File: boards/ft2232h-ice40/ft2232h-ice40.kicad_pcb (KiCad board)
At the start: 4 copper layers, 34 x 22.4 mm, 36 parts, among them J1 USB_B_Micro, J2 Conn_01x08, U1 AP7361C_SOT-89-5, U2 FT2232H, X1 ASEM1-12.000MHZ

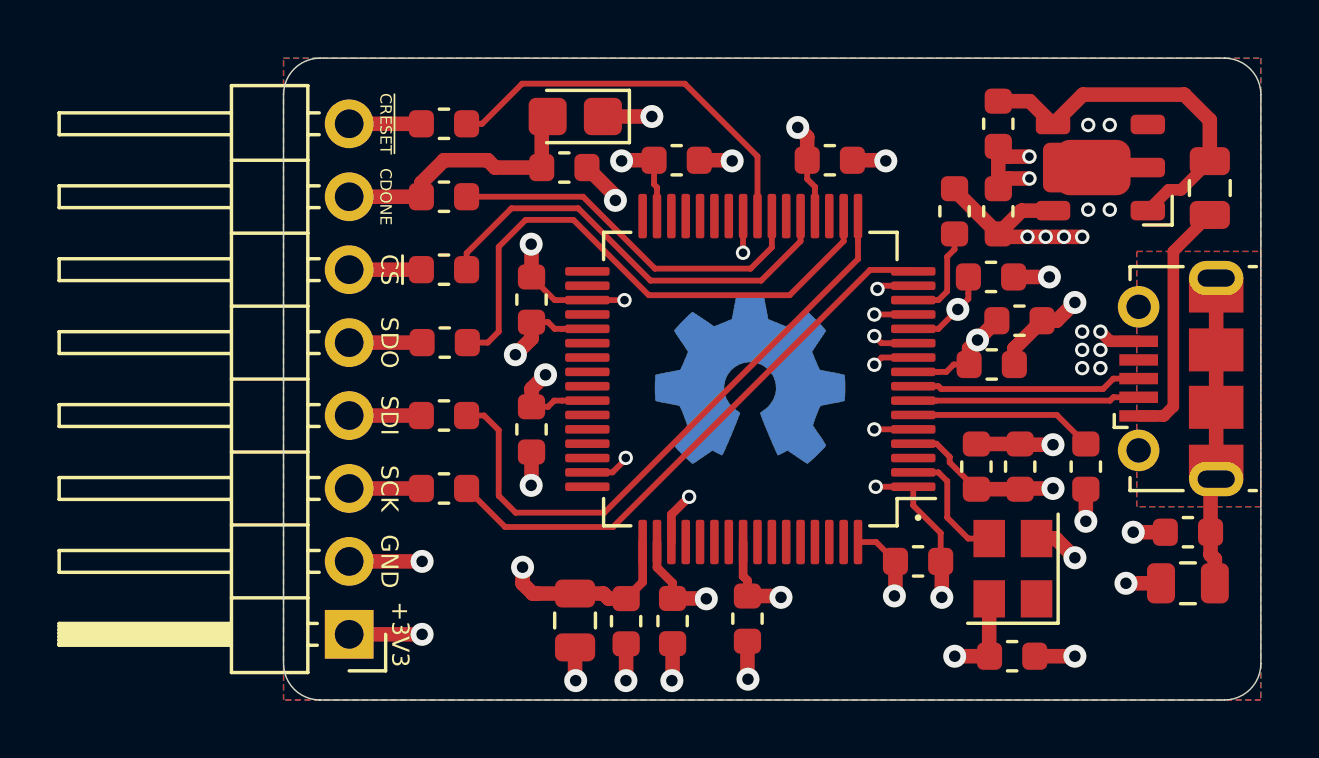
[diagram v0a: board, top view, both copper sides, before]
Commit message: Minor tweaks to signal layout.
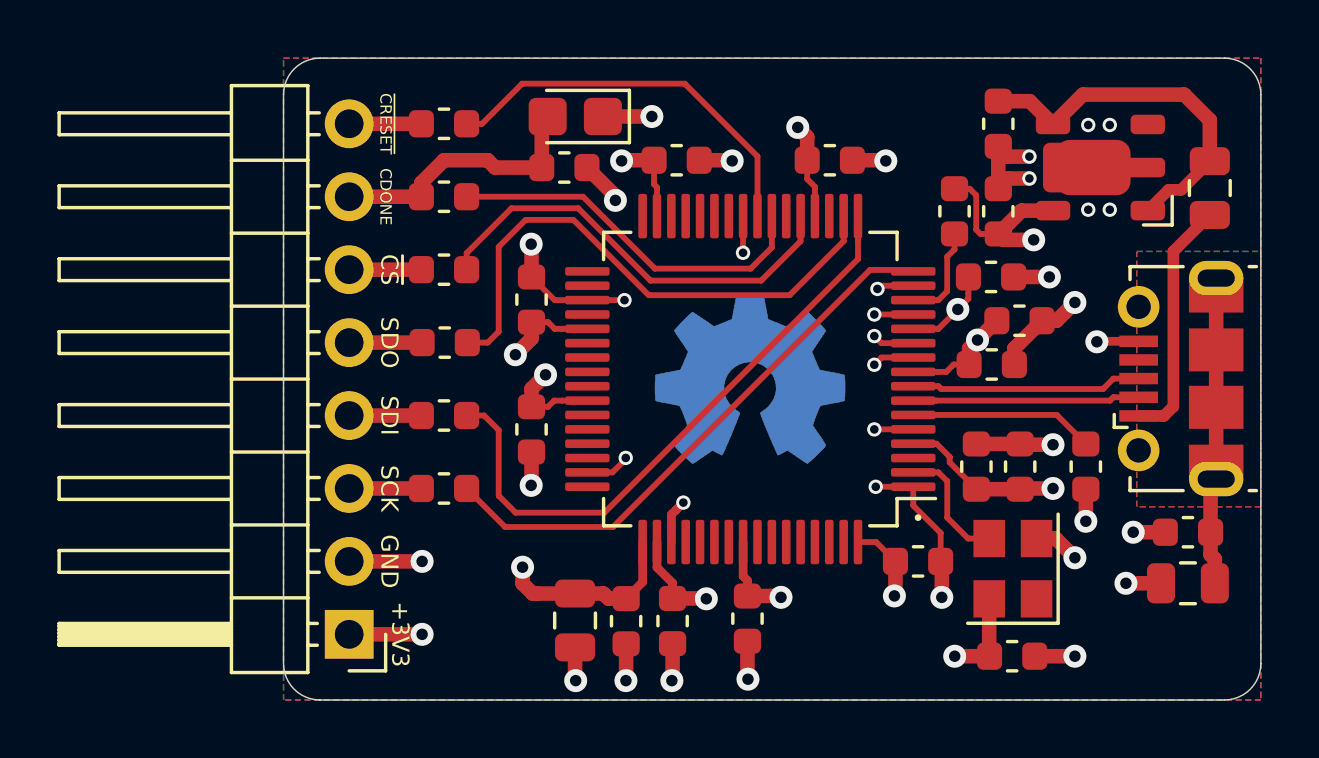
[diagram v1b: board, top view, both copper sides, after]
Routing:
- net +3V3: track 40.7 -> 39.7 mm, vias 14 -> 11
- net GND: track 55.5 -> 55.2 mm, vias 41 -> 36
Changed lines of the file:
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@@
     (thickness 1.6)
     (drawings 17)
-    (tracks 310)
+    (tracks 305)
     (zones 0)
     (modules 36)
@@
   )
   (setup
-    (last_trace_width 0.508)
+    (last_trace_width 0.2032)
     (user_trace_width 0.2032)
     (user_trace_width 0.3048)
@@
   (segment (start 76.2 26.416) (end 76.835 25.781) (width 0.508) (layer F.Cu) (net 1))
   (segment (start 75.692 26.416) (end 76.2 26.416) (width 0.508) (layer F.Cu) (net 1))
-  (via (at 77.724 28.067) (size 0.5) (drill 0.3) (layers F.Cu B.Cu) (net 1))
-  (via (at 77.724 27.432) (size 0.5) (drill 0.3) (layers F.Cu B.Cu) (net 1))
-  (via (at 77.089 26.797) (size 0.5) (drill 0.3) (layers F.Cu B.Cu) (net 1))
-  (via (at 77.089 27.432) (size 0.5) (drill 0.3) (layers F.Cu B.Cu) (net 1))
-  (via (at 77.089 28.067) (size 0.5) (drill 0.3) (layers F.Cu B.Cu) (net 1))
-  (via (at 77.724 26.797) (size 0.5) (drill 0.3) (layers F.Cu B.Cu) (net 1))
-  (segment (start 78.059 27.132) (end 79.0555 27.132) (width 0.4064) (layer F.Cu) (net 1))
-  (segment (start 77.724 26.797) (end 78.059 27.132) (width 0.4064) (layer F.Cu) (net 1))
   (segment (start 63.289999 32.740001) (end 63.290001 32.740001) (width 0.2032) (layer F.Cu) (net 1))
   (segment (start 60.732 31.698) (end 61.193611 31.236389) (width 0.2032) (layer F.Cu) (net 1))
@@
   (segment (start 65.432 37.5775) (end 65.432 38.882) (width 0.508) (layer F.Cu) (net 1))
   (segment (start 65.432 38.882) (end 65.45 38.9) (width 0.508) (layer F.Cu) (net 1))
+  (via (at 77.6 27.15) (size 0.8) (drill 0.4) (layers F.Cu B.Cu) (net 1))
+  (segment (start 77.618 27.132) (end 77.6 27.15) (width 0.3048) (layer F.Cu) (net 1))
+  (segment (start 79.0555 27.132) (end 77.618 27.132) (width 0.3048) (layer F.Cu) (net 1))
+  (via (at 63.2 32.75) (size 0.5) (drill 0.3) (layers F.Cu B.Cu) (net 1))
   (segment (start 62.782 34.123) (end 62.782 33.168) (width 0.3048) (layer F.Cu) (net 1))
-  (segment (start 62.782 33.168) (end 63.4 32.55) (width 0.3048) (layer F.Cu) (net 1))
-  (segment (start 63.4 32.55) (end 63.4 32.55) (width 0.3048) (layer F.Cu) (net 1))
-  (via (at 63.4 32.55) (size 0.5) (drill 0.3) (layers F.Cu B.Cu) (net 1))
+  (segment (start 62.950001 32.999999) (end 63.2 32.75) (width 0.3048) (layer F.Cu) (net 1))
+  (segment (start 62.782 33.168) (end 62.950001 32.999999) (width 0.3048) (layer F.Cu) (net 1))
   (segment (start 69.9115 34.123) (end 70.5865 34.798) (width 0.2032) (layer F.Cu) (net 2))
   (segment (start 69.282 34.123) (end 69.9115 34.123) (width 0.2032) (layer F.Cu) (net 2))
@@
   (segment (start 74.9795 22.582) (end 74.168 23.3935) (width 0.508) (layer F.Cu) (net 4))
   (segment (start 76.074 22.582) (end 74.9795 22.582) (width 0.508) (layer F.Cu) (net 4))
-  (segment (start 72.644 21.8695) (end 74.168 23.3935) (width 0.508) (layer F.Cu) (net 4))
-  (segment (start 72.644 21.8185) (end 72.644 21.8695) (width 0.508) (layer F.Cu) (net 4))
   (segment (start 72.082 28.198) (end 71.207 28.198) (width 0.2032) (layer F.Cu) (net 4))
   (segment (start 72.356501 28.198) (end 72.082 28.198) (width 0.2032) (layer F.Cu) (net 4))
@@
   (segment (start 60.833 22.0725) (end 59.8425 21.082) (width 0.508) (layer F.Cu) (net 4))
   (segment (start 60.833 22.225) (end 60.833 22.0725) (width 0.508) (layer F.Cu) (net 4))
-  (via (at 75.184 23.495) (size 0.5) (drill 0.3) (layers F.Cu B.Cu) (net 4))
-  (via (at 75.819 23.495) (size 0.5) (drill 0.3) (layers F.Cu B.Cu) (net 4))
-  (via (at 76.454 23.495) (size 0.5) (drill 0.3) (layers F.Cu B.Cu) (net 4))
-  (via (at 77.089 23.495) (size 0.5) (drill 0.3) (layers F.Cu B.Cu) (net 4))
-  (segment (start 74.2695 23.495) (end 74.168 23.3935) (width 0.508) (layer F.Cu) (net 4))
-  (segment (start 77.089 23.495) (end 74.2695 23.495) (width 0.508) (layer F.Cu) (net 4))
   (via (at 67.183008 19.685) (size 0.8) (drill 0.4) (layers F.Cu B.Cu) (net 4))
   (segment (start 67.513 20.014992) (end 67.183008 19.685) (width 0.508) (layer F.Cu) (net 4))
@@
   (segment (start 65.432 36.0025) (end 65.432 35.465) (width 0.3048) (layer F.Cu) (net 4))
   (segment (start 65.432 35.465) (end 65.282 35.315) (width 0.3048) (layer F.Cu) (net 4))
+  (via (at 75.4 23.6) (size 0.8) (drill 0.4) (layers F.Cu B.Cu) (net 4))
+  (segment (start 75.4 23.6) (end 74.3745 23.6) (width 0.508) (layer F.Cu) (net 4))
+  (segment (start 74.3745 23.6) (end 74.168 23.3935) (width 0.508) (layer F.Cu) (net 4))
+  (segment (start 73.1685 21.8185) (end 72.644 21.8185) (width 0.2032) (layer F.Cu) (net 4))
+  (segment (start 73.4 22.05) (end 73.1685 21.8185) (width 0.2032) (layer F.Cu) (net 4))
+  (segment (start 73.4 23.25) (end 73.4 22.05) (width 0.2032) (layer F.Cu) (net 4))
+  (segment (start 74.168 23.3935) (end 73.5435 23.3935) (width 0.2032) (layer F.Cu) (net 4))
+  (segment (start 73.5435 23.3935) (end 73.4 23.25) (width 0.2032) (layer F.Cu) (net 4))
   (segment (start 79.9337 29.732) (end 80.264 29.4017) (width 0.4064) (layer F.Cu) (net 5))
   (segment (start 79.0555 29.732) (end 79.9337 29.732) (width 0.4064) (layer F.Cu) (net 5))
